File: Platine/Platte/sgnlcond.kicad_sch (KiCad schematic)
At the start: 0 parts

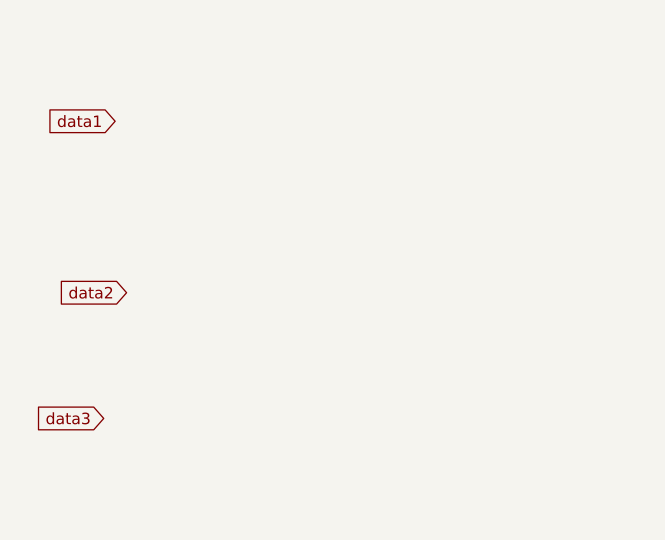
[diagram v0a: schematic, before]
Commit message: adding signal conditioning phase to plate PCB
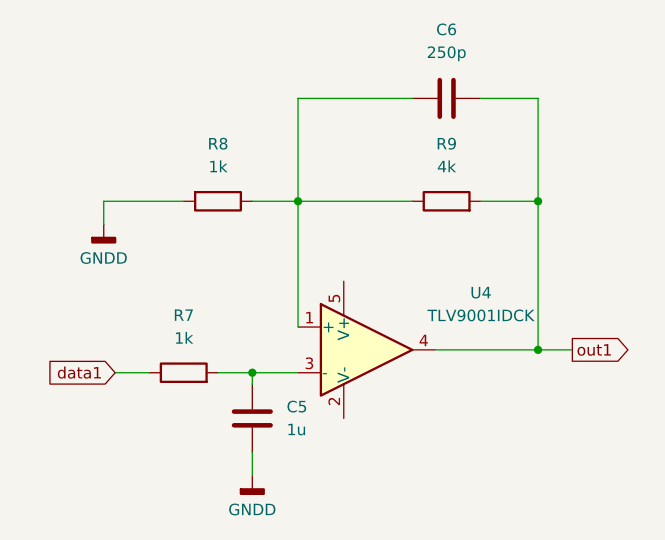
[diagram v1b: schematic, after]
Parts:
- added C5: 1u, symbol Device:C
- added C6: 250p, symbol Device:C
- added R7, R8: 1k, symbol Device:R
- added R9: 4k, symbol Device:R
- added U4: TLV9001IDCK, Package_TO_SOT_SMD:SOT-353_SC-70-5, symbol Amplifier_Operational:TLV9001IDCK
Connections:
- net data1: now also R7.1
- new net: C5.1, R7.2, U4.3 (-)
- new net: C6.1, R8.1, R9.1, U4.1 (+)
- new net GNDD: C5.2, R8.2
- new net out1: C6.2, R9.2, U4.4

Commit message: not much
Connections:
- net GNDD: now also U4.2 (V-)
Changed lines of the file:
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@@
+	)
+	(junction
+		(at 66.04 74.93)
+		(diameter 0)
+		(color 0 0 0 0)
 	)
 	(junction
@@
 		(pts
 			(xy 66.04 64.77) (xy 66.04 66.04)
+		)
+		(stroke
+			(width 0)
+			(type default)
+		)
+	)
+	(wire
+		(pts
+			(xy 76.2 69.85) (xy 76.2 74.93)
 		)
 		(stroke
@@
 	(wire
 		(pts
+			(xy 66.04 74.93) (xy 66.04 76.2)
+		)
+		(stroke
+			(width 0)
+			(type default)
+		)
+	)
+	(wire
+		(pts
+			(xy 66.04 74.93) (xy 76.2 74.93)
+		)
+		(stroke
+			(width 0)
+			(type default)
+		)
+	)
+	(wire
+		(pts
 			(xy 86.36 62.23) (xy 97.79 62.23)
 		)
@@
 	(wire
 		(pts
-			(xy 66.04 73.66) (xy 66.04 76.2)
+			(xy 66.04 73.66) (xy 66.04 74.93)
 		)
 		(stroke

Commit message: ok
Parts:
- removed U4: TLV9001IDCK, Package_TO_SOT_SMD:SOT-353_SC-70-5, symbol Amplifier_Operational:TLV9001IDCK
- added C2, C4: 10n, Capacitor_SMD:C_0201_0603Metric_Pad0.64x0.40mm_HandSolder, symbol Device:C
- added C3, C7: 300p, Capacitor_SMD:C_0201_0603Metric_Pad0.64x0.40mm_HandSolder, symbol Device:C
- added R10, R11, R4, R5: 1k, Resistor_SMD:R_0201_0603Metric_Pad0.64x0.40mm_HandSolder, symbol Device:R
- added R12, R6: 3.3k, Resistor_SMD:R_0201_0603Metric_Pad0.64x0.40mm_HandSolder, symbol Device:R
- added U5: ~, symbol TLV9004:TLV900
- C5: value 1u -> 10n; footprint (none) -> Capacitor_SMD:C_0201_0603Metric_Pad0.64x0.40mm_HandSolder
- C6: value 250p -> 300p; footprint (none) -> Capacitor_SMD:C_0201_0603Metric_Pad0.64x0.40mm_HandSolder
- R7, R8: footprint (none) -> Resistor_SMD:R_0201_0603Metric_Pad0.64x0.40mm_HandSolder
- R9: value 4k -> 3.3k; footprint (none) -> Resistor_SMD:R_0201_0603Metric_Pad0.64x0.40mm_HandSolder
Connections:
- net GNDD: now also C2.2, C4.2, R11.2, R5.2, U5.11 (V-)
- net out1: now also U5.1 (OUT1)
- net Vin1+: now reaches C5.1, R7.2
- net Vin1+: now also U5.3 (IN1+)
- net Vin1-: now reaches C6.1, R8.1, R9.1
- net Vin1-: now also U5.2 (IN1-)
- new net +3.3VA: U5.4 (V+)
- new net Vin2+: C2.1, R4.2, U5.6 (IN2-)
- new net Vin2-: C3.1, R5.1, R6.1, U5.5 (IN2+)
- new net Vin3+: C4.1, R10.2, U5.10 (IN3+)
- new net Vin3-: C7.1, R11.1, R12.1, U5.9 (IN3-)
- new net data2: R4.1
- new net data3: R10.1
- new net out2: C3.2, R6.2, U5.7 (OUT2)
- new net out3: C7.2, R12.2, U5.8 (OUT3)
- no-connect marks 0 -> 3
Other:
- note added: "Cut frequency: 20 kHz Voltage gain: 3.3"
- moved on the sheet: C6, R8, R9

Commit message: plate pcb almost finished
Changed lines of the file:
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@@
 		)
 	)
-	(global_label "out1"
+	(hierarchical_label "out2"
+		(shape output)
+		(at 90.17 106.68 0)
+		(fields_autoplaced yes)
+		(effects
+			(font
+				(size 1.27 1.27)
+			)
+			(justify left)
+		)
+	)
+	(hierarchical_label "data1"
+		(shape input)
+		(at 50.8 64.77 180)
+		(fields_autoplaced yes)
+		(effects
+			(font
+				(size 1.27 1.27)
+			)
+			(justify right)
+		)
+	)
+	(hierarchical_label "out1"
+		(shape output)
+		(at 146.05 44.45 180)
+		(fields_autoplaced yes)
+		(effects
+			(font
+				(size 1.27 1.27)
+			)
+			(justify right)
+		)
+	)
+	(hierarchical_label "out1"
 		(shape output)
 		(at 90.17 62.23 0)
@@
 			(justify left)
 		)
-		(property "Intersheetrefs" "${INTERSHEET_REFS}"
-			(at 97.3884 62.23 0)
-			(effects
-				(font
-					(size 1.27 1.27)
-				)
-				(justify left)
-				(hide yes)
-			)
-		)
 	)
-	(global_label "out1"
-		(shape output)
-		(at 146.05 44.45 180)
-		(fields_autoplaced yes)
-		(effects
-			(font
-				(size 1.27 1.27)
-			)
-			(justify right)
-		)
-		(property "Intersheetrefs" "${INTERSHEET_REFS}"
-			(at 138.8316 44.45 0)
-			(effects
-				(font
-					(size 1.27 1.27)
-				)
-				(justify right)
-				(hide yes)
-			)
-		)
-	)
-	(global_label "out3"
+	(hierarchical_label "out3"
 		(shape output)
 		(at 185.42 72.39 0)
@@
 			(justify left)
 		)
-		(property "Intersheetrefs" "${INTERSHEET_REFS}"
-			(at 192.6384 72.39 0)
-			(effects
-				(font
-					(size 1.27 1.27)
-				)
-				(justify left)
-				(hide yes)
+	)
+	(hierarchical_label "out2"
+		(shape output)
+		(at 146.05 72.39 180)
+		(fields_autoplaced yes)
+		(effects
+			(font
+				(size 1.27 1.27)
 			)
+			(justify right)
 		)
 	)
-	(global_label "out3"
+	(hierarchical_label "data2"
+		(shape input)
+		(at 50.8 109.22 180)
+		(fields_autoplaced yes)
+		(effects
+			(font
+				(size 1.27 1.27)
+			)
+			(justify right)
+		)
+	)
+	(hierarchical_label "out3"
 		(shape output)
 		(at 91.44 154.94 0)
@@
 			(justify left)
 		)
-		(property "Intersheetrefs" "${INTERSHEET_REFS}"
-			(at 98.6584 154.94 0)
-			(effects
-				(font
-					(size 1.27 1.27)
-				)
-				(justify left)
-				(hide yes)
-			)
-		)
 	)
-	(global_label "out2"
-		(shape output)
-		(at 146.05 72.39 180)
-		(fields_autoplaced yes)
-		(effects
-			(font
-				(size 1.27 1.27)
-			)
-			(justify right)
-		)
-		(property "Intersheetrefs" "${INTERSHEET_REFS}"
-			(at 138.8316 72.39 0)
-			(effects
-				(font
-					(size 1.27 1.27)
-				)
-				(justify right)
-				(hide yes)
-			)
-		)
-	)
-	(global_label "data1"
-		(shape input)
-		(at 50.8 64.77 180)
-		(fields_autoplaced yes)
-		(effects
-			(font
-				(size 1.27 1.27)
-			)
-			(justify right)
-		)
-		(property "Intersheetrefs" "${INTERSHEET_REFS}"
-			(at 42.4326 64.77 0)
-			(effects
-				(font
-					(size 1.27 1.27)
-				)
-				(justify right)
-				(hide yes)
-			)
-		)
-	)
-	(global_label "data3"
+	(hierarchical_label "data3"
 		(shape input)
 		(at 52.07 157.48 180)
@@
 			(justify right)
 		)
-		(property "Intersheetrefs" "${INTERSHEET_REFS}"
-			(at 43.7026 157.48 0)
-			(effects
-				(font
-					(size 1.27 1.27)
-				)
-				(justify right)
-				(hide yes)
-			)
-		)
 	)
-	(global_label "out2"
-		(shape output)
-		(at 90.17 106.68 0)
-		(fields_autoplaced yes)
-		(effects
-			(font
-				(size 1.27 1.27)
-			)
-			(justify left)
-		)
-		(property "Intersheetrefs" "${INTERSHEET_REFS}"
-			(at 97.3884 106.68 0)
-			(effects
-				(font
-					(size 1.27 1.27)
-				)
-				(justify left)
-				(hide yes)
-			)
-		)
-	)
-	(global_label "data2"
-		(shape input)
-		(at 50.8 109.22 180)
-		(fields_autoplaced yes)
-		(effects
-			(font
-				(size 1.27 1.27)
-			)
-			(justify right)
-		)
-		(property "Intersheetrefs" "${INTERSHEET_REFS}"
-			(at 42.4326 109.22 0)
-			(effects
-				(font
-					(size 1.27 1.27)
-				)
-				(justify right)
-				(hide yes)
-			)
-		)
-	)
